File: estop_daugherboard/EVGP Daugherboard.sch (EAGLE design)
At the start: 32 parts, among them J1 E-STOP HEADER, J2 AVR_SPI_PROG_3X2PTH, J3 UX60-MB-5S8, U1 ATMEGA32U4-AU, U4 NL27WZ08USG, X1 TSX-3225 16.0000MF18X-AC0

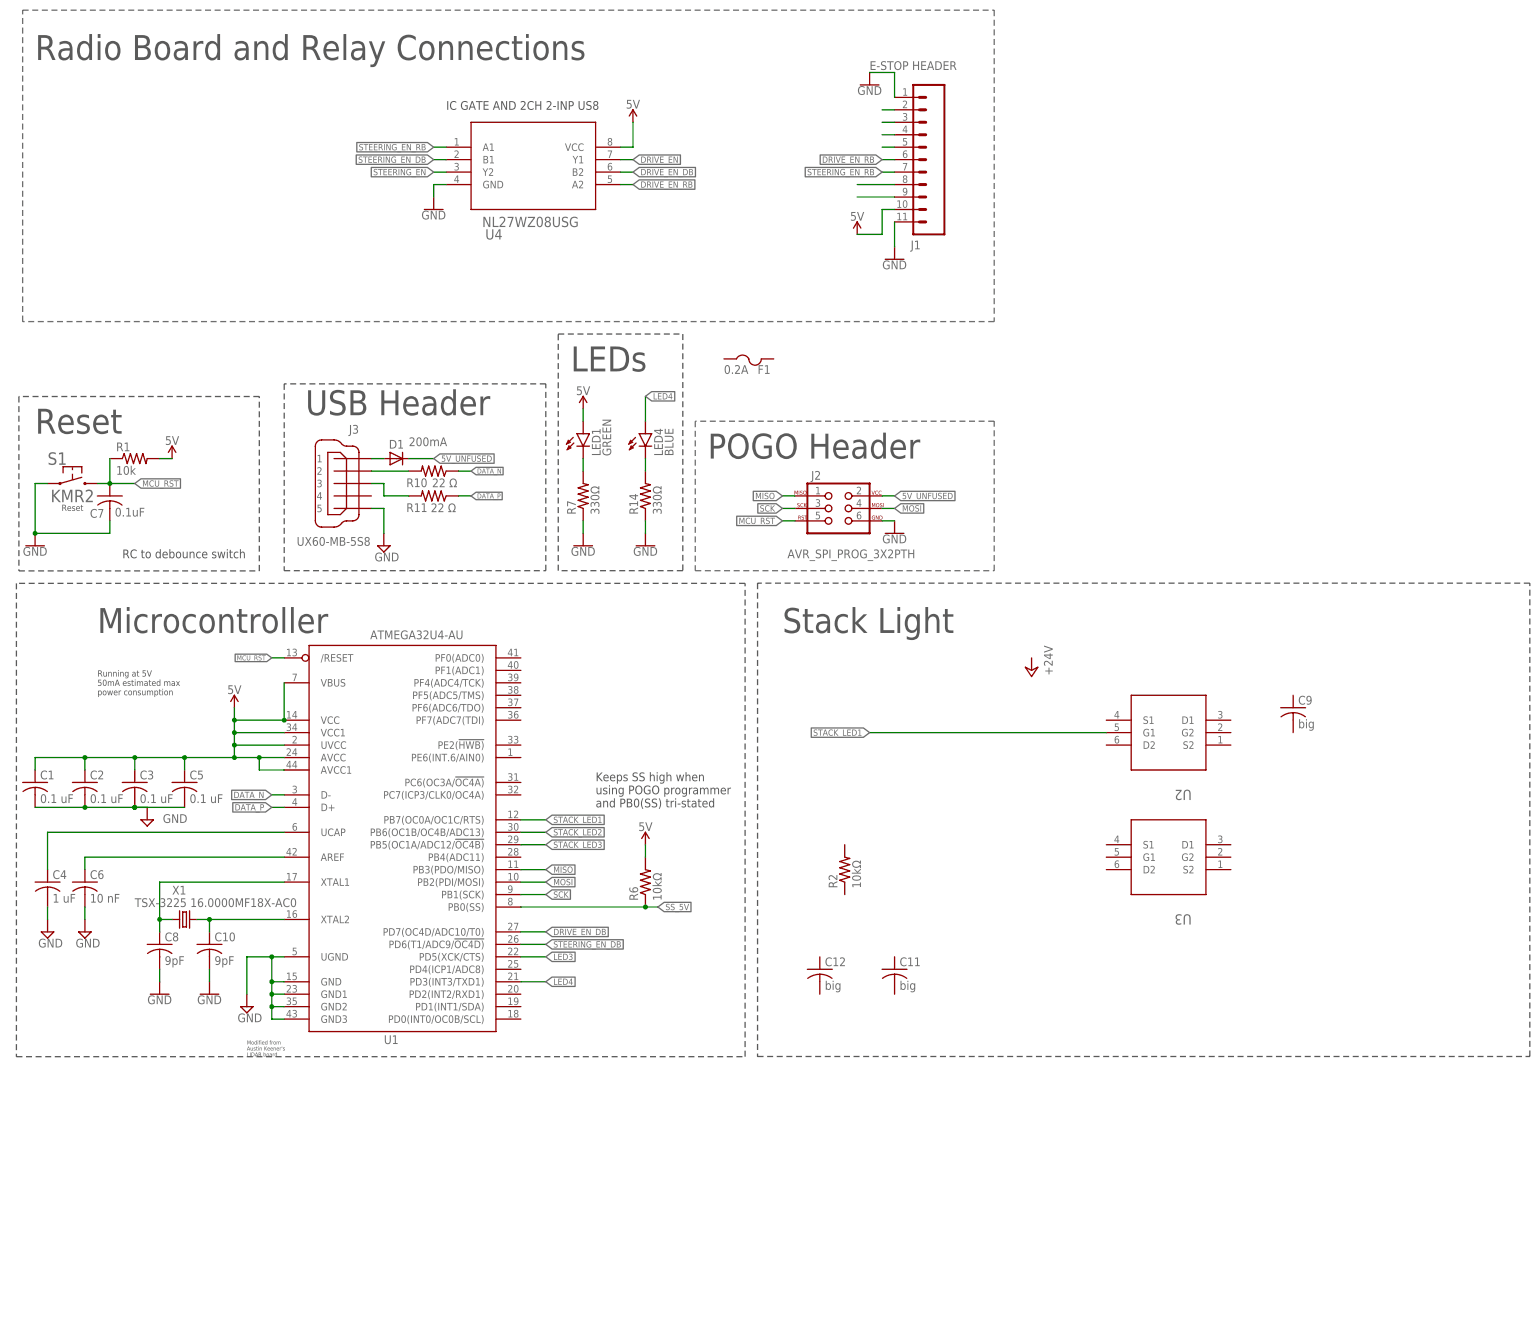
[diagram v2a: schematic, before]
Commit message: Integrated Ethernet POE module connection and stack light into the main schematic
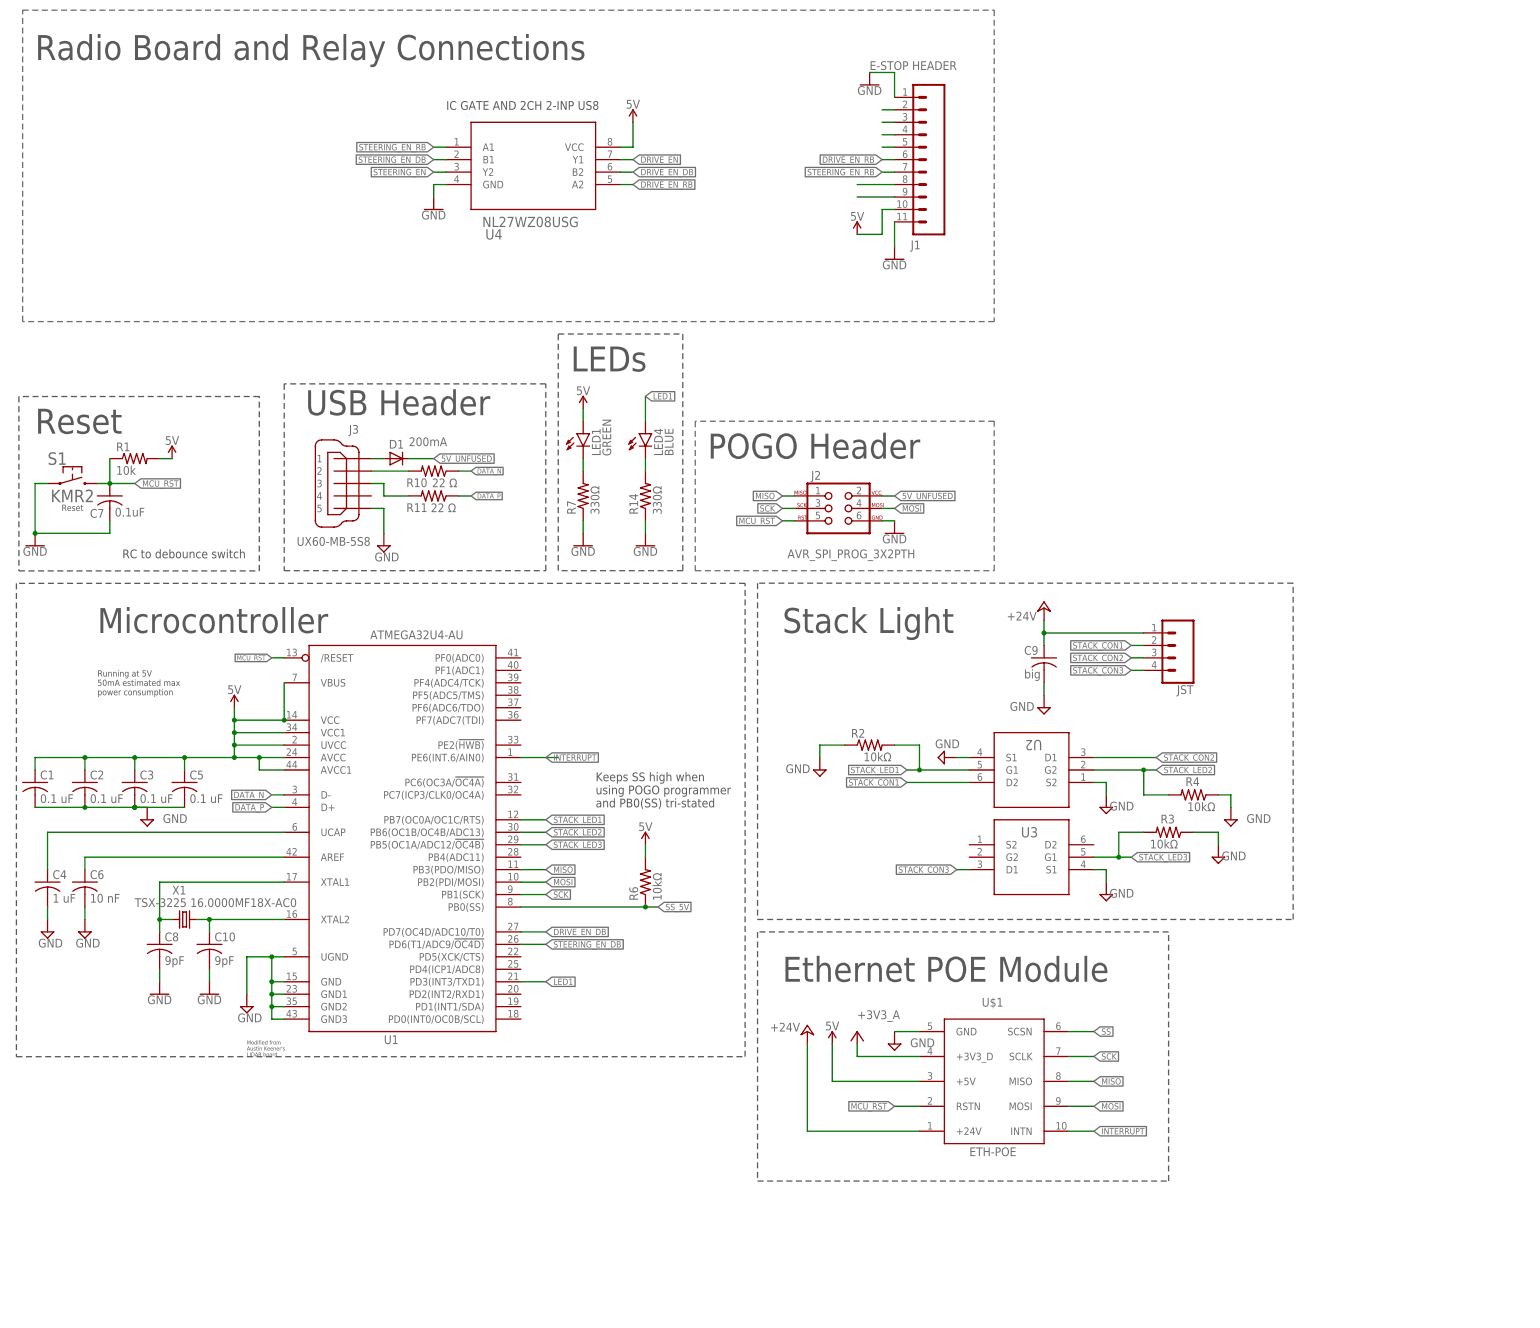
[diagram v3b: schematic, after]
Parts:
- removed C11, C12: big, resistor:C-USC0603
- removed F1: 0.2A, adafruit:PTCFUSE-1206
- added JST: (no value), SparkFun-Connectors:CONN_04JST-PTH
- added R3, R4: 10kΩ, rcl:R-US_R0603
- added U$1: ETH-POE, ethernet_poe:ETH-POE
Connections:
- net LED4 renamed LED1
- removed net LED3: U1.PD5(XCK/CTS)
- new net +24V: C9.1, JST.1, U$1.+24V
- new net +3V3_A: U$1.+3V3_D
- new net INTERRUPT: U$1.INTN, U1.PE6(INT.6/AIN0)
- new net SS: U$1.SCSN
- new net STACK_CON1: JST.2, U2.D2
- new net STACK_CON2: JST.3, U2.D1
- new net STACK_CON3: JST.4, U3.D1
- net 5V: now also U$1.+5V
- net GND: now also C9.2, R2.1, R3.1, R4.1, U$1.GND, U2.S1, U2.S2, U3.S1
- net MCU_RST: now also U$1.RSTN
- net MISO: now also U$1.MISO
- net MOSI: now also U$1.MOSI
- net SCK: now also U$1.SCLK
- net STACK_LED1: now also R2.2
- net STACK_LED2: now also R4.2, U2.G2
- net STACK_LED3: now also R3.2, U3.G1
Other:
- note added: "Ethernet POE Module"
- moved on the sheet: C9, R2, U2, U3

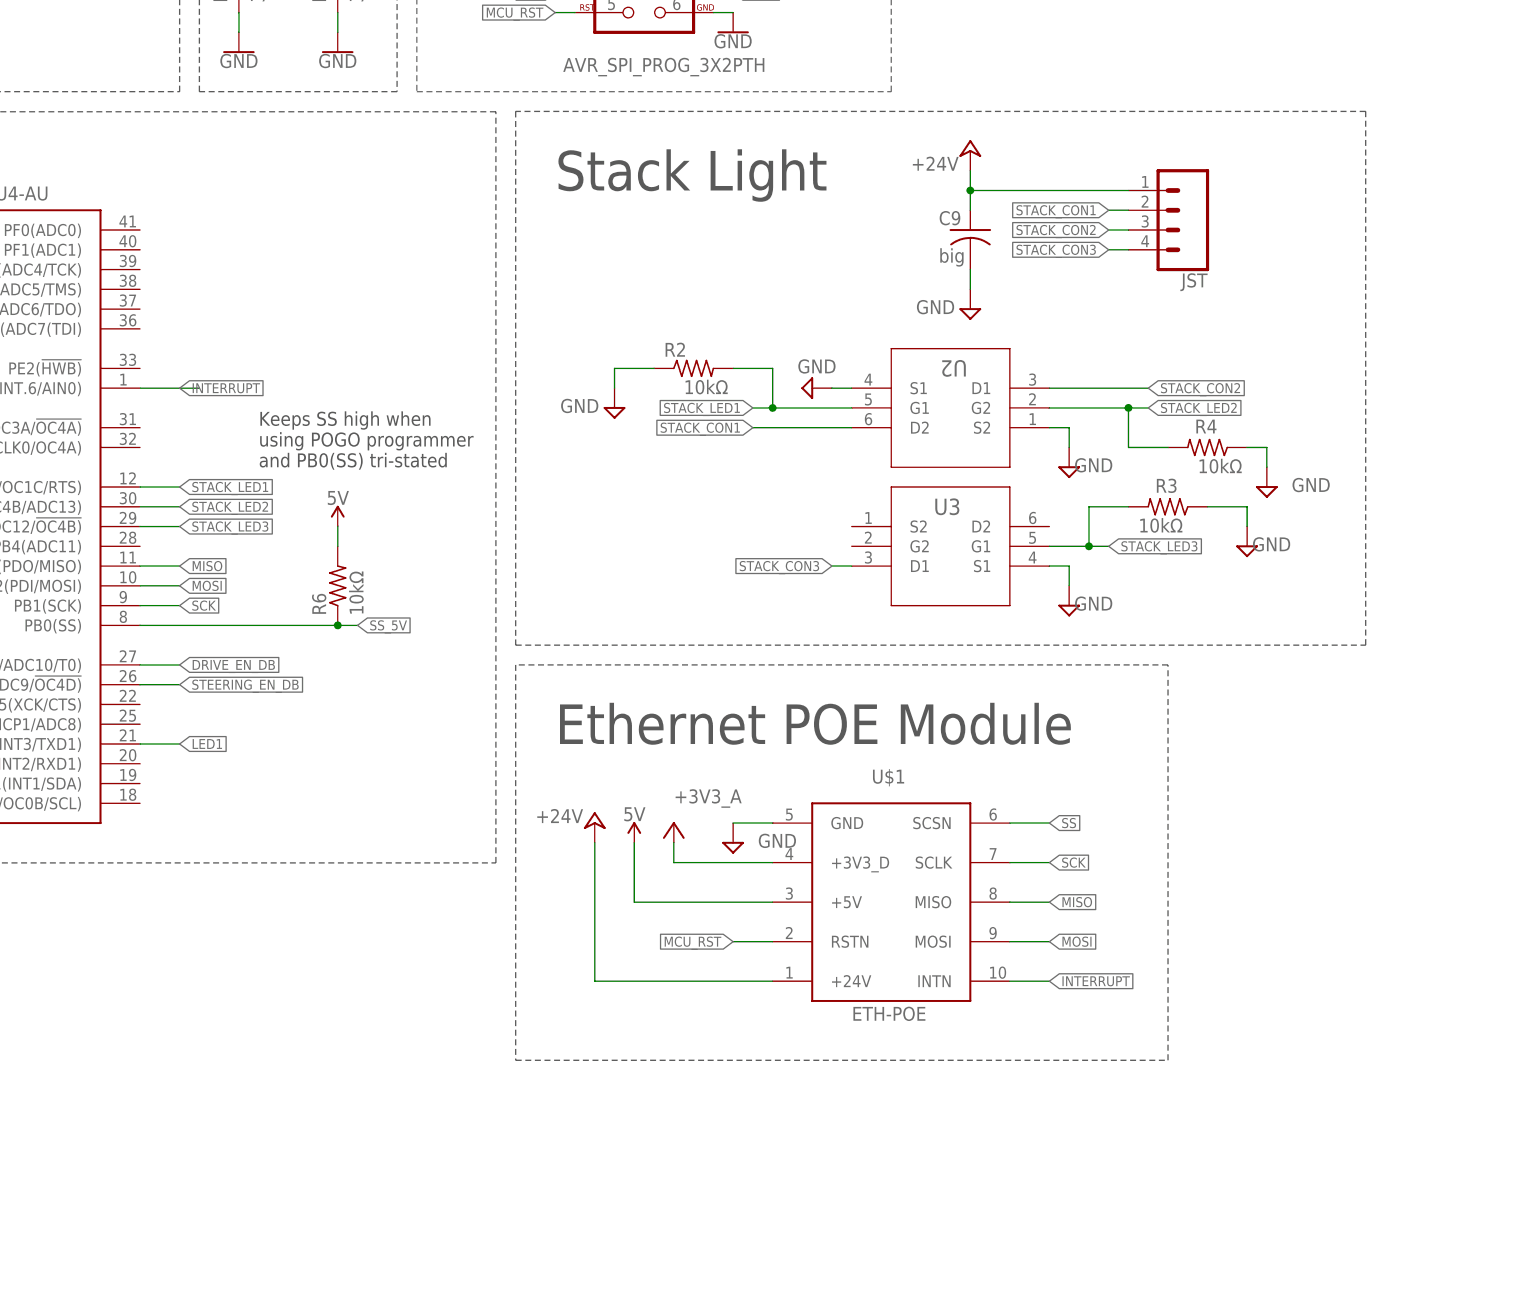
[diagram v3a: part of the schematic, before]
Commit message: Fixed the power stuff on the ethernet poe module
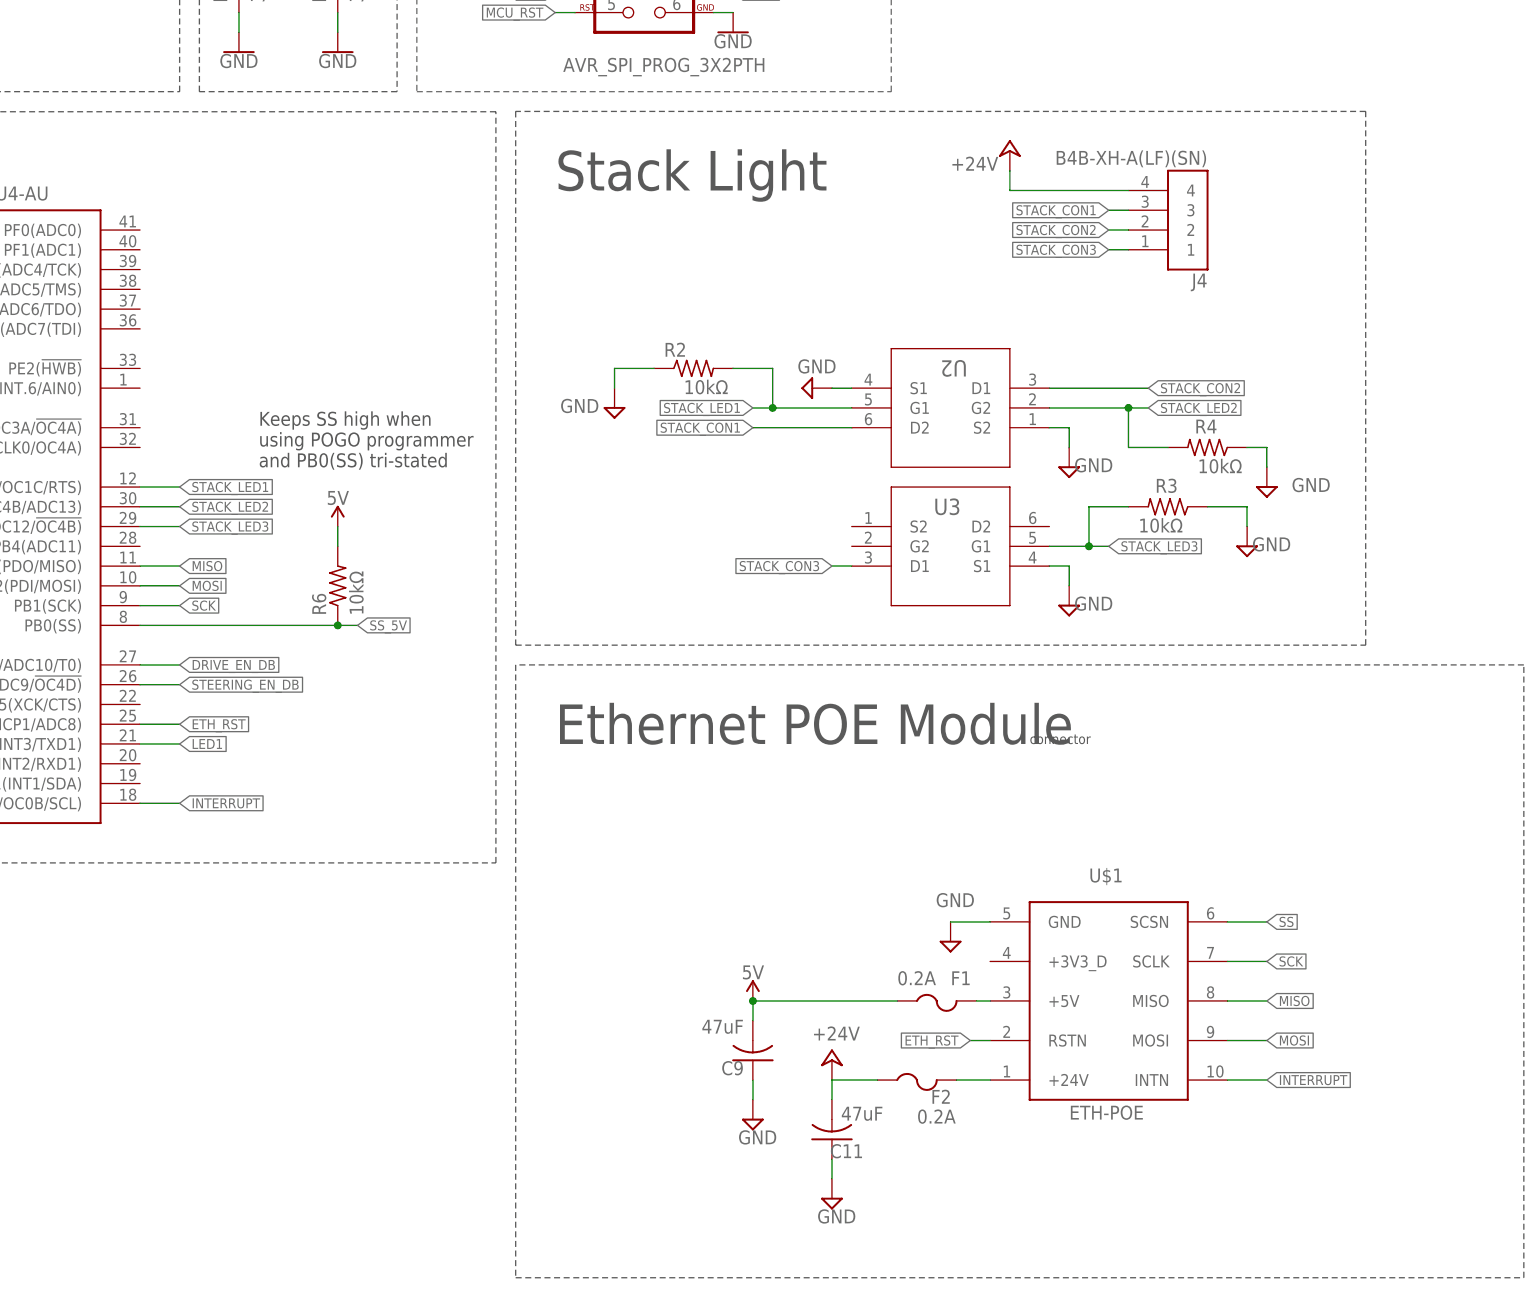
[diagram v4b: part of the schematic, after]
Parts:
- removed JST: (no value), SparkFun-Connectors:CONN_04JST-PTH
- added C11: 47uF, resistor:C-USC0603
- added F1, F2: 0.2A, adafruit:PTCFUSE-1206
- added J4: B4B-XH-A(LF)(SN), JST-XH-Connector:B4B-XH-A(LF)(SN)
- C9: value big -> 47uF
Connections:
- removed net +3V3_A: U$1.+3V3_D
- new net ETH_RST: U$1.RSTN, U1.PD4(ICP1/ADC8)
- new net N$2: F1.2, U$1.+5V
- new net N$4: F2.2, U$1.+24V
- net +24V: now also C11.2, F2.1, J4.4; no longer C9.1, JST.1, U$1.+24V
- net 5V: now also C9.2, F1.1; no longer U$1.+5V
- net GND: now also C11.1, C9.1; no longer C9.2
- net INTERRUPT: now also U1.PD0(INT0/OC0B/SCL); no longer U1.PE6(INT.6/AIN0)
- net MCU_RST: no longer U$1.RSTN
- net STACK_CON1: now also J4.3; no longer JST.2
- net STACK_CON2: now also J4.2; no longer JST.3
- net STACK_CON3: now also J4.1; no longer JST.4
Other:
- note added: "connector"
- moved on the sheet: C9, U$1
